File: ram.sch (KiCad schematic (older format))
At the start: 1 part, among them U1 LFE5U-85F-6BG381C

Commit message: More fixes
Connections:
- net GN14 renamed LTDC_FROM_FPGA_DE
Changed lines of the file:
@@
 SDRAM_nCS
 Text GLabel 10050 4650 2    60   Input ~ 0
-GN14
+LTDC_FROM_FPGA_DE
 Text GLabel 10050 5450 2    60   Input ~ 0
 GN15

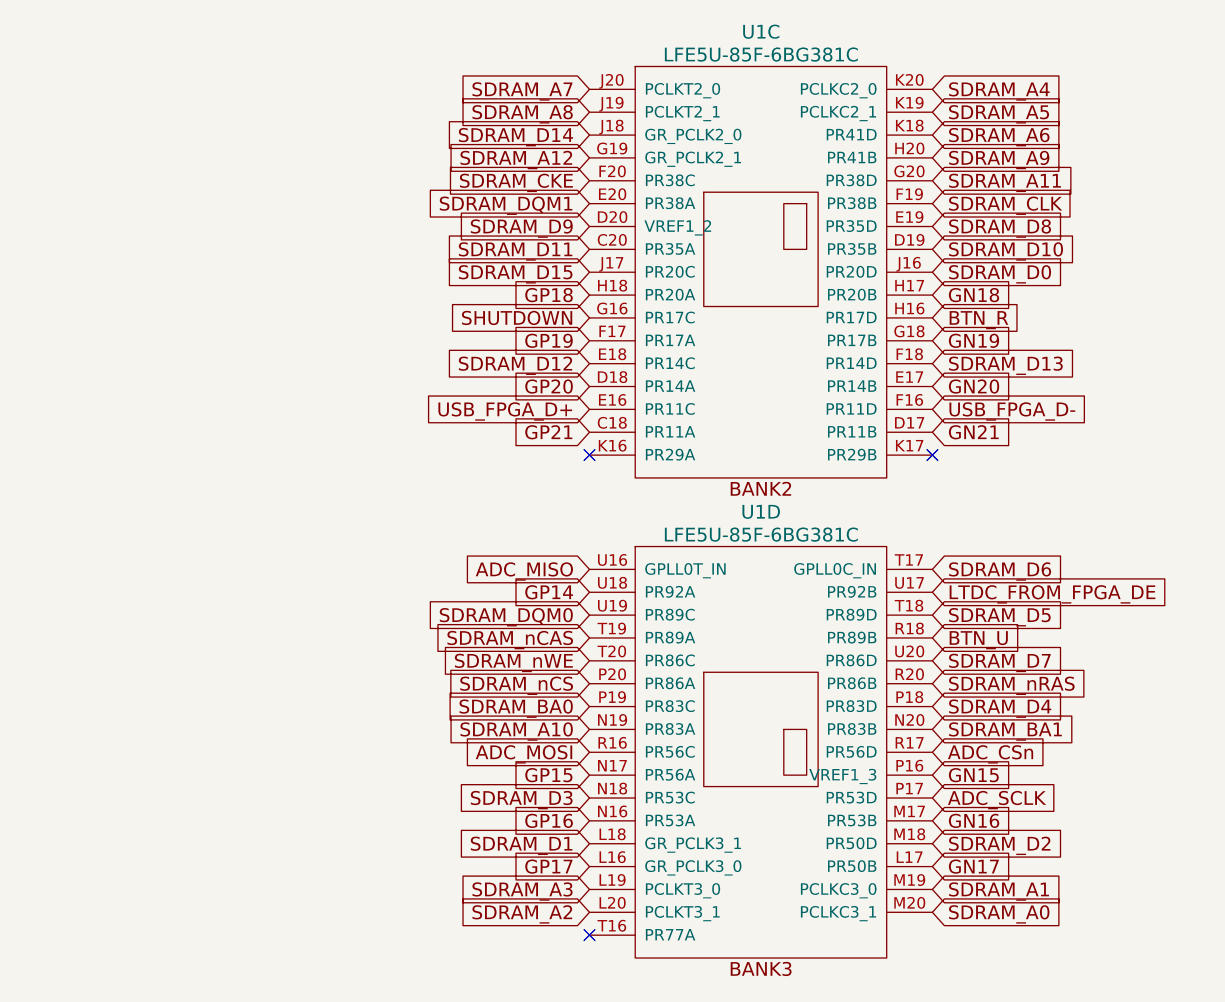
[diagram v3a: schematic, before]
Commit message: Adding all SPI to FPGA resorting LCD TO FPGA
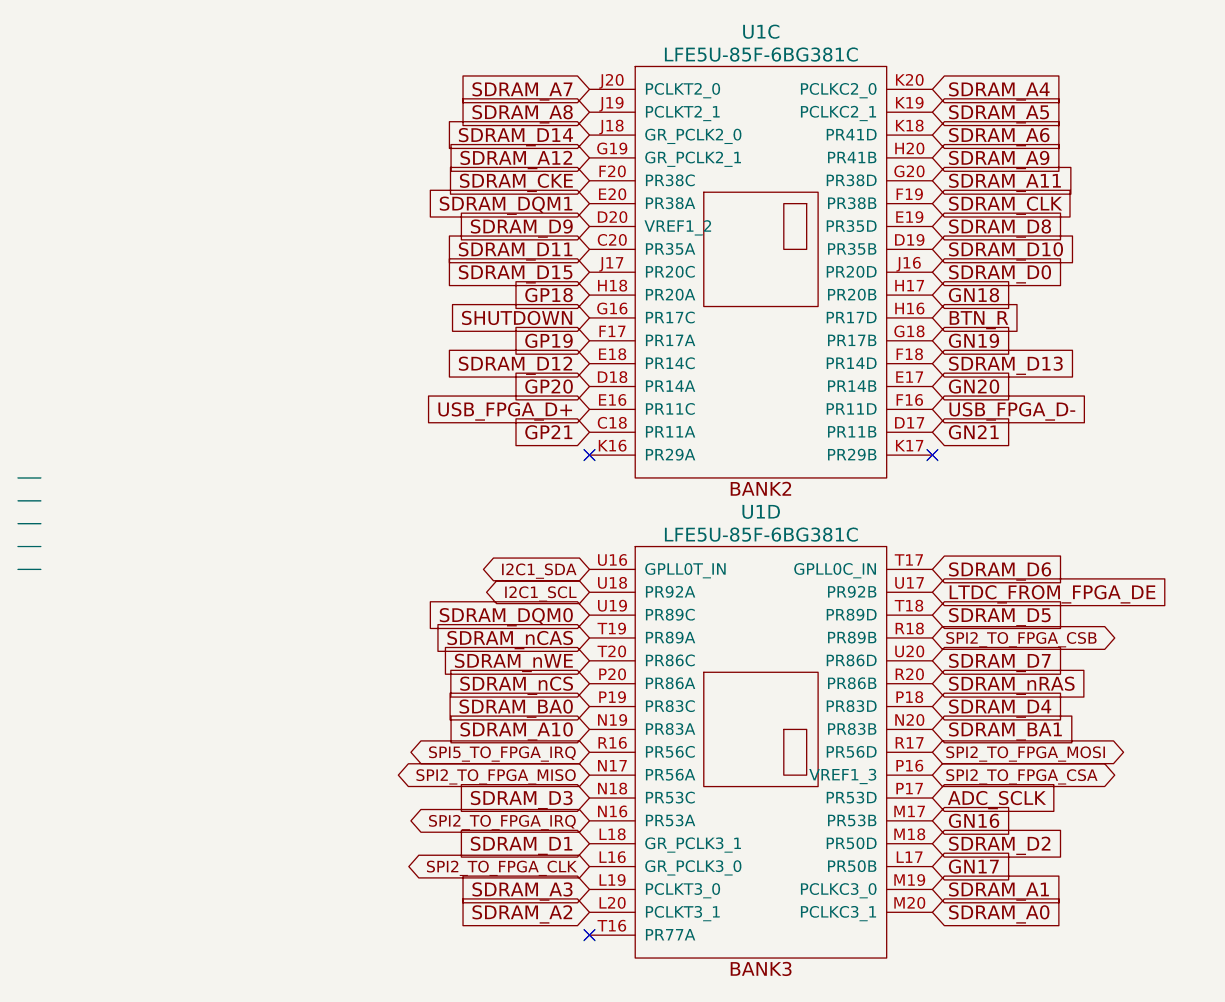
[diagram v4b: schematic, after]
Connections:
- net labels added: I2C1_SCL, I2C1_SDA, SPI2_TO_FPGA_CLK, SPI2_TO_FPGA_CSA, SPI2_TO_FPGA_CSB, SPI2_TO_FPGA_IRQ, SPI2_TO_FPGA_MISO, SPI2_TO_FPGA_MOSI, SPI5_TO_FPGA_IRQ
- net labels removed: ADC_CSn, ADC_MISO, ADC_MOSI, BTN_U, GN15, GP14, GP15, GP16, GP17
- wire segments 0 -> 5
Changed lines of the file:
@@
 Text GLabel 10050 4650 2    60   Input ~ 0
 LTDC_FROM_FPGA_DE
-Text GLabel 10050 5450 2    60   Input ~ 0
-GN15
-Text GLabel 8550 5450 0    60   Input ~ 0
-GP15
-Text GLabel 8550 4650 0    60   Input ~ 0
-GP14
-Text GLabel 8550 5650 0    60   Input ~ 0
-GP16
 Text GLabel 10050 5650 2    60   Input ~ 0
 GN16
@@
 Text GLabel 10050 5850 2    60   Input ~ 0
 GN17
-Text GLabel 8550 5850 0    60   Input ~ 0
-GP17
-Text GLabel 8550 4550 0    60   Input ~ 0
-ADC_MISO
-Text GLabel 8550 5350 0    60   Input ~ 0
-ADC_MOSI
-Text GLabel 10050 5350 2    60   Input ~ 0
-ADC_CSn
 Text GLabel 10050 5550 2    60   Input ~ 0
 ADC_SCLK
@@
 Text GLabel 8550 3450 0    60   Input ~ 0
 SHUTDOWN
-Text GLabel 10050 4850 2    60   Input ~ 0
-BTN_U
 Text GLabel 10050 3450 2    60   Input ~ 0
 BTN_R
@@
 NoConn ~ 10050 4050
 NoConn ~ 8550 6150
+Text GLabel 8550 5650 0    50   BiDi ~ 0
+SPI2_TO_FPGA_IRQ
+Text GLabel 8550 5350 0    50   BiDi ~ 0
+SPI5_TO_FPGA_IRQ
+Text GLabel 10050 5450 2    50   BiDi ~ 0
+SPI2_TO_FPGA_CSA
+Text GLabel 8550 4650 0    50   BiDi ~ 0
+I2C1_SCL
+Text GLabel 8550 4550 0    50   BiDi ~ 0
+I2C1_SDA
+Text GLabel 8550 5450 0    50   BiDi ~ 0
+SPI2_TO_FPGA_MISO
+Text GLabel 10050 4850 2    50   BiDi ~ 0
+SPI2_TO_FPGA_CSB
+Text GLabel 8550 5850 0    50   BiDi ~ 0
+SPI2_TO_FPGA_CLK
+Text GLabel 10050 5350 2    50   BiDi ~ 0
+SPI2_TO_FPGA_MOSI
+Wire Wire Line
+	6150 4550 6050 4550
+Wire Wire Line
+	6150 4450 6050 4450
+Wire Wire Line
+	6150 4350 6050 4350
+Wire Wire Line
+	6150 4250 6050 4250
+Wire Wire Line
+	6050 4150 6150 4150
 $EndSCHEMATC

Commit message: Adding SPI from FPGA
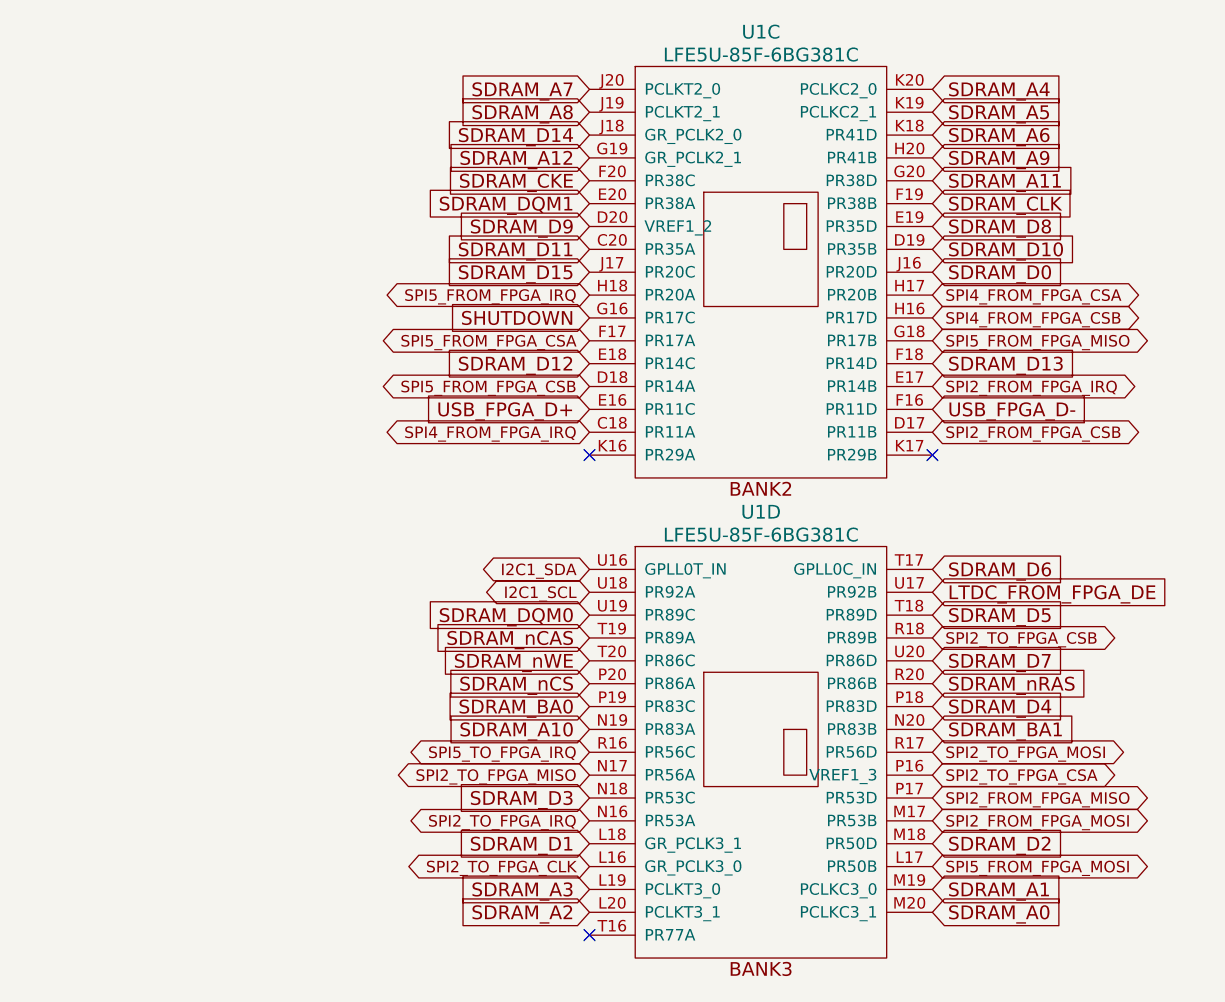
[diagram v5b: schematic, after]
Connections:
- net labels added: SPI2_FROM_FPGA_CSB, SPI2_FROM_FPGA_IRQ, SPI2_FROM_FPGA_MISO, SPI2_FROM_FPGA_MOSI, SPI4_FROM_FPGA_CSA, SPI4_FROM_FPGA_CSB, SPI4_FROM_FPGA_IRQ, SPI5_FROM_FPGA_CSA, SPI5_FROM_FPGA_CSB, SPI5_FROM_FPGA_IRQ, SPI5_FROM_FPGA_MISO, SPI5_FROM_FPGA_MOSI
- net labels removed: ADC_SCLK, BTN_R, GN16, GN17, GN18, GN19, GN20, GN21, GP18, GP19, GP20, GP21
- wire segments 5 -> 0
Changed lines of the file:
@@
 Text GLabel 10050 5150 2    60   Input ~ 0
 SDRAM_D4
-Text GLabel 10050 4750 2    60   Input ~ 0
-SDRAM_D5
 Text GLabel 10050 4550 2    60   Input ~ 0
 SDRAM_D6
@@
 Text GLabel 10050 4650 2    60   Input ~ 0
 LTDC_FROM_FPGA_DE
-Text GLabel 10050 5650 2    60   Input ~ 0
-GN16
-Text GLabel 10050 3350 2    60   Input ~ 0
-GN18
-Text GLabel 10050 3950 2    60   Input ~ 0
-GN21
-Text GLabel 10050 3750 2    60   Input ~ 0
-GN20
-Text GLabel 8550 3350 0    60   Input ~ 0
-GP18
-Text GLabel 8550 3950 0    60   Input ~ 0
-GP21
-Text GLabel 8550 3750 0    60   Input ~ 0
-GP20
-Text GLabel 10050 3550 2    60   Input ~ 0
-GN19
-Text GLabel 8550 3550 0    60   Input ~ 0
-GP19
-Text GLabel 10050 5850 2    60   Input ~ 0
-GN17
-Text GLabel 10050 5550 2    60   Input ~ 0
-ADC_SCLK
 Text GLabel 8550 3850 0    60   Input ~ 0
 USB_FPGA_D+
@@
 Text GLabel 8550 3450 0    60   Input ~ 0
 SHUTDOWN
-Text GLabel 10050 3450 2    60   Input ~ 0
-BTN_R
 NoConn ~ 8550 4050
 NoConn ~ 10050 4050
@@
 Text GLabel 10050 5350 2    50   BiDi ~ 0
 SPI2_TO_FPGA_MOSI
-Wire Wire Line
-	6150 4550 6050 4550
-Wire Wire Line
-	6150 4450 6050 4450
-Wire Wire Line
-	6150 4350 6050 4350
-Wire Wire Line
-	6150 4250 6050 4250
-Wire Wire Line
-	6050 4150 6150 4150
+Text GLabel 8550 3350 0    50   BiDi ~ 0
+SPI5_FROM_FPGA_IRQ
+Text GLabel 8550 3550 0    50   BiDi ~ 0
+SPI5_FROM_FPGA_CSA
+Text GLabel 8550 3750 0    50   BiDi ~ 0
+SPI5_FROM_FPGA_CSB
+Text GLabel 8550 3950 0    50   BiDi ~ 0
+SPI4_FROM_FPGA_IRQ
+Text GLabel 10050 3450 2    50   BiDi ~ 0
+SPI4_FROM_FPGA_CSB
+Text GLabel 10050 3750 2    50   BiDi ~ 0
+SPI2_FROM_FPGA_IRQ
+Text GLabel 10050 3950 2    50   BiDi ~ 0
+SPI2_FROM_FPGA_CSB
+Text GLabel 10050 5550 2    50   BiDi ~ 0
+SPI2_FROM_FPGA_MISO
+Text GLabel 10050 5650 2    50   BiDi ~ 0
+SPI2_FROM_FPGA_MOSI
+Text GLabel 10050 3550 2    50   BiDi ~ 0
+SPI5_FROM_FPGA_MISO
+Text GLabel 10050 5850 2    50   BiDi ~ 0
+SPI5_FROM_FPGA_MOSI
+Text GLabel 10050 3350 2    50   BiDi ~ 0
+SPI4_FROM_FPGA_CSA
+Text GLabel 10050 4750 2    60   Input ~ 0
+SDRAM_D5
 $EndSCHEMATC

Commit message: Routing FPGA to LCD
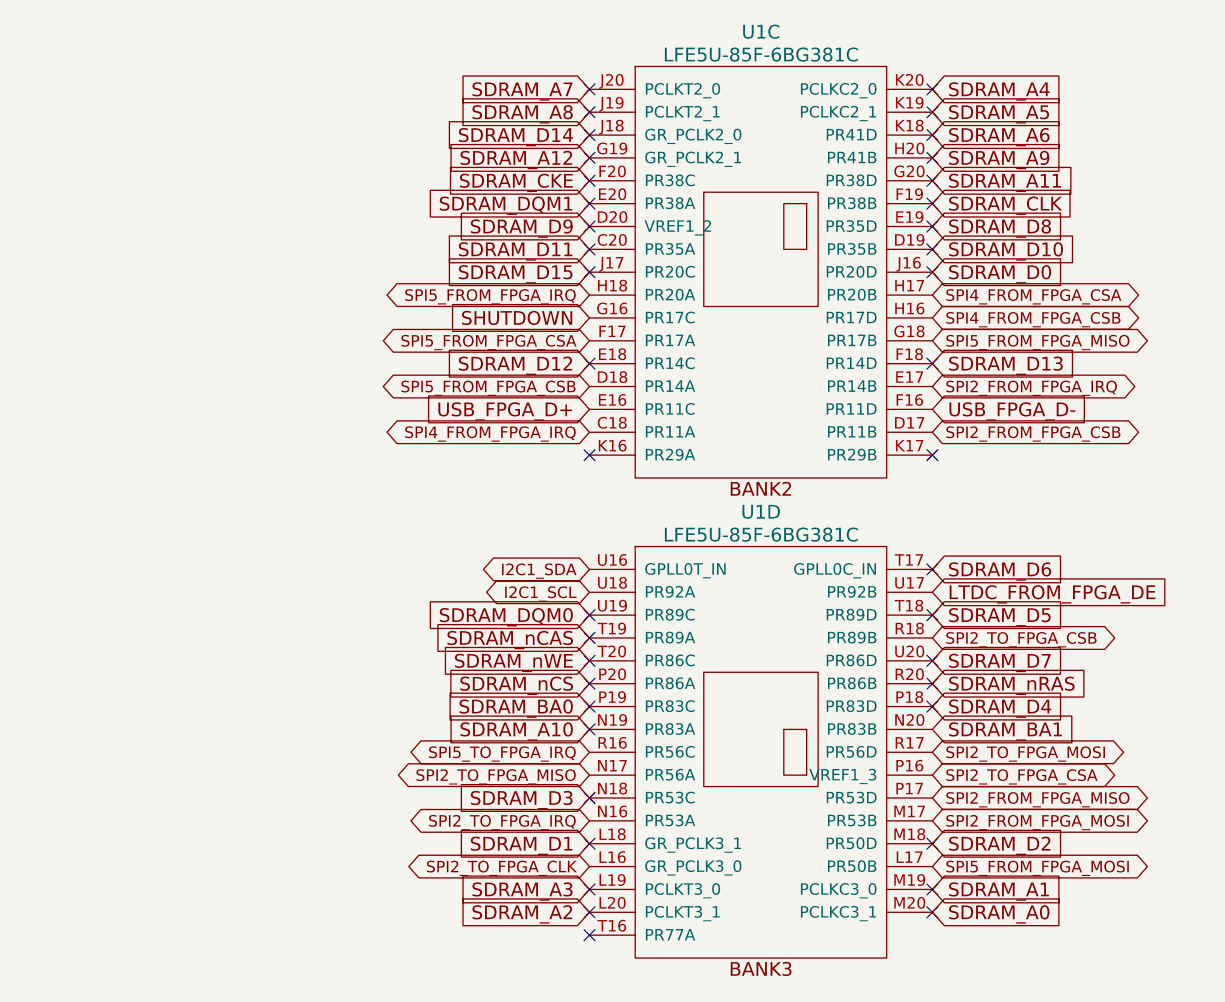
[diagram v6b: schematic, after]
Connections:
- no-connect marks 3 -> 41
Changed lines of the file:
@@
 Text GLabel 10050 4750 2    60   Input ~ 0
 SDRAM_D5
+NoConn ~ 8550 2450
+NoConn ~ 8550 2550
+NoConn ~ 8550 2650
+NoConn ~ 8550 2750
+NoConn ~ 8550 2850
+NoConn ~ 8550 2950
+NoConn ~ 8550 3050
+NoConn ~ 8550 3150
+NoConn ~ 8550 3250
+NoConn ~ 8550 3650
+NoConn ~ 10050 3650
+NoConn ~ 10050 3250
+NoConn ~ 10050 3150
+NoConn ~ 10050 3050
+NoConn ~ 10050 2950
+NoConn ~ 10050 2850
+NoConn ~ 10050 2750
+NoConn ~ 10050 2650
+NoConn ~ 10050 2550
+NoConn ~ 10050 2450
+NoConn ~ 8550 4750
+NoConn ~ 8550 4850
+NoConn ~ 8550 4950
+NoConn ~ 8550 5050
+NoConn ~ 8550 5150
+NoConn ~ 8550 5250
+NoConn ~ 8550 5550
+NoConn ~ 8550 5750
+NoConn ~ 8550 5950
+NoConn ~ 8550 6050
+NoConn ~ 10050 6050
+NoConn ~ 10050 5950
+NoConn ~ 10050 5750
+NoConn ~ 10050 5150
+NoConn ~ 10050 5050
+NoConn ~ 10050 4950
+NoConn ~ 10050 4750
+NoConn ~ 10050 4550
 $EndSCHEMATC

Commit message: Routing long signals
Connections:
- net SPI2_FROM_FPGA_MOSI: now also U1.L17 (PR50B); no longer U1.M17 (PR53B)
- net SPI5_FROM_FPGA_MOSI: now also U1.M17 (PR53B); no longer U1.L17 (PR50B)
- net SPI2_TO_FPGA_CLK renamed SPI5_FROM_FPGA_CLK
- net SPI2_TO_FPGA_CSB: no longer names the net of U1.R18 (PR89B)
- net SPI2_TO_FPGA_IRQ: no longer names the net of U1.N16 (PR53A)
- net SPI5_TO_FPGA_IRQ: no longer names the net of U1.R16 (PR56C)
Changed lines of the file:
@@
 NoConn ~ 10050 4050
 NoConn ~ 8550 6150
-Text GLabel 8550 5650 0    50   BiDi ~ 0
-SPI2_TO_FPGA_IRQ
-Text GLabel 8550 5350 0    50   BiDi ~ 0
-SPI5_TO_FPGA_IRQ
 Text GLabel 10050 5450 2    50   BiDi ~ 0
 SPI2_TO_FPGA_CSA
@@
 Text GLabel 8550 5450 0    50   BiDi ~ 0
 SPI2_TO_FPGA_MISO
-Text GLabel 10050 4850 2    50   BiDi ~ 0
-SPI2_TO_FPGA_CSB
-Text GLabel 8550 5850 0    50   BiDi ~ 0
-SPI2_TO_FPGA_CLK
 Text GLabel 10050 5350 2    50   BiDi ~ 0
 SPI2_TO_FPGA_MOSI
-Text GLabel 8550 3350 0    50   BiDi ~ 0
-SPI5_FROM_FPGA_IRQ
 Text GLabel 8550 3550 0    50   BiDi ~ 0
 SPI5_FROM_FPGA_CSA
@@
 Text GLabel 10050 5550 2    50   BiDi ~ 0
 SPI2_FROM_FPGA_MISO
-Text GLabel 10050 5650 2    50   BiDi ~ 0
-SPI2_FROM_FPGA_MOSI
 Text GLabel 10050 3550 2    50   BiDi ~ 0
 SPI5_FROM_FPGA_MISO
-Text GLabel 10050 5850 2    50   BiDi ~ 0
+Text GLabel 10050 5650 2    50   BiDi ~ 0
 SPI5_FROM_FPGA_MOSI
 Text GLabel 10050 3350 2    50   BiDi ~ 0
@@
 NoConn ~ 10050 4750
 NoConn ~ 10050 4550
+Text GLabel 8550 5850 0    50   BiDi ~ 0
+SPI5_FROM_FPGA_CLK
+Text GLabel 8550 3350 0    50   BiDi ~ 0
+SPI5_FROM_FPGA_IRQ
+Text GLabel 10050 5850 2    50   BiDi ~ 0
+SPI2_FROM_FPGA_MOSI
 $EndSCHEMATC
